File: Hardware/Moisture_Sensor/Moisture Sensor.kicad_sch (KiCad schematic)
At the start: 24 parts, among them J1 Conn_01x02_Pin, J2 Conn_01x02_Pin, J3 Conn_01x03_Pin, Q1 BSS123, Q2 BSS84, U1 ESP32-H2-SUPERMINI, U3 NE555D

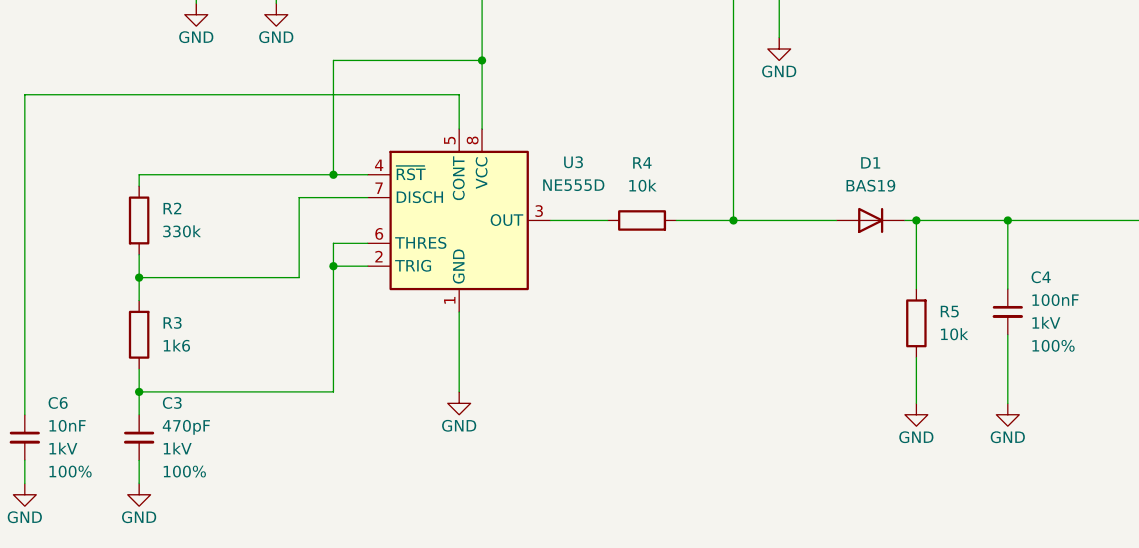
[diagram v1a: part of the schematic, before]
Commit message: R2 auf 330 geändert und R5 auf 1Meg
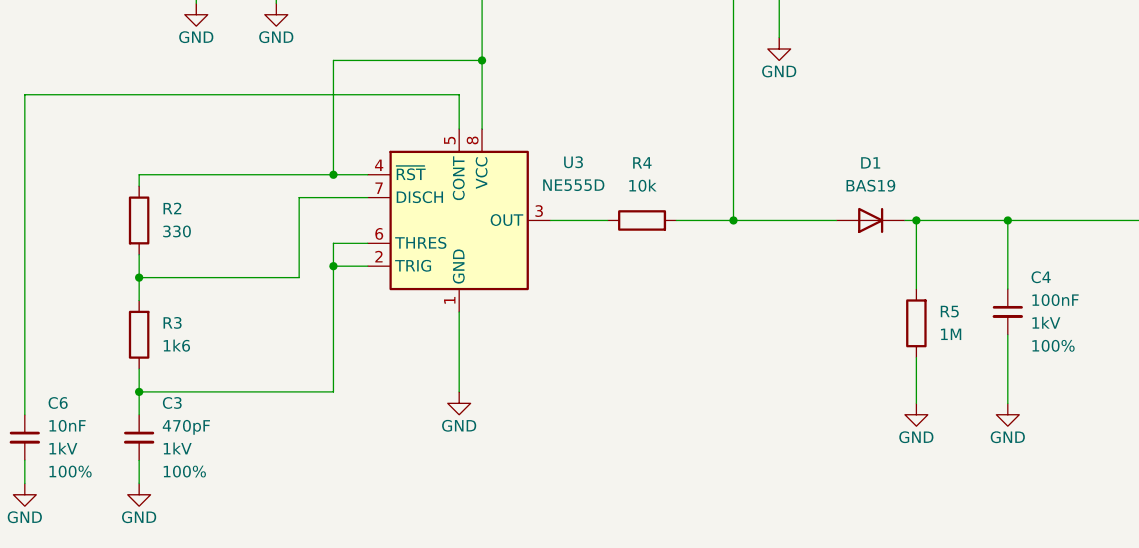
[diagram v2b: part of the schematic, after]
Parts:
- R2: value 330k -> 330
- R5: value 10k -> 1M
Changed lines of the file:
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@@
 			)
 		)
-		(property "Value" "330k"
+		(property "Value" "330"
 			(at 40.64 162.5599 0)
 			(effects
@@
 			)
 		)
-		(property "Value" "10k"
+		(property "Value" "1M"
 			(at 127 173.9899 0)
 			(effects

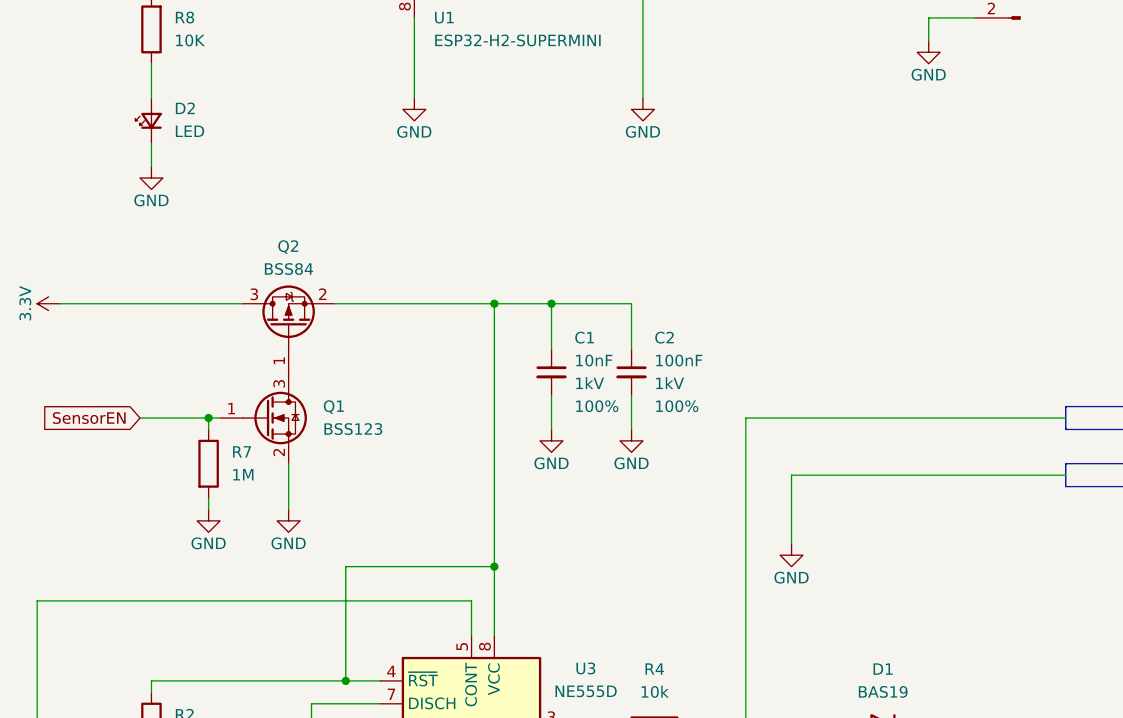
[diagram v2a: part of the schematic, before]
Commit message: Fehler im Schlatplan!!! R7, Q1 und Q2 nicht bestücken. Verbindung von Q1/pin1 zu Q2/Pin2 wie eingezeichnet herstellen und mit GPIO ein und ausschalten.
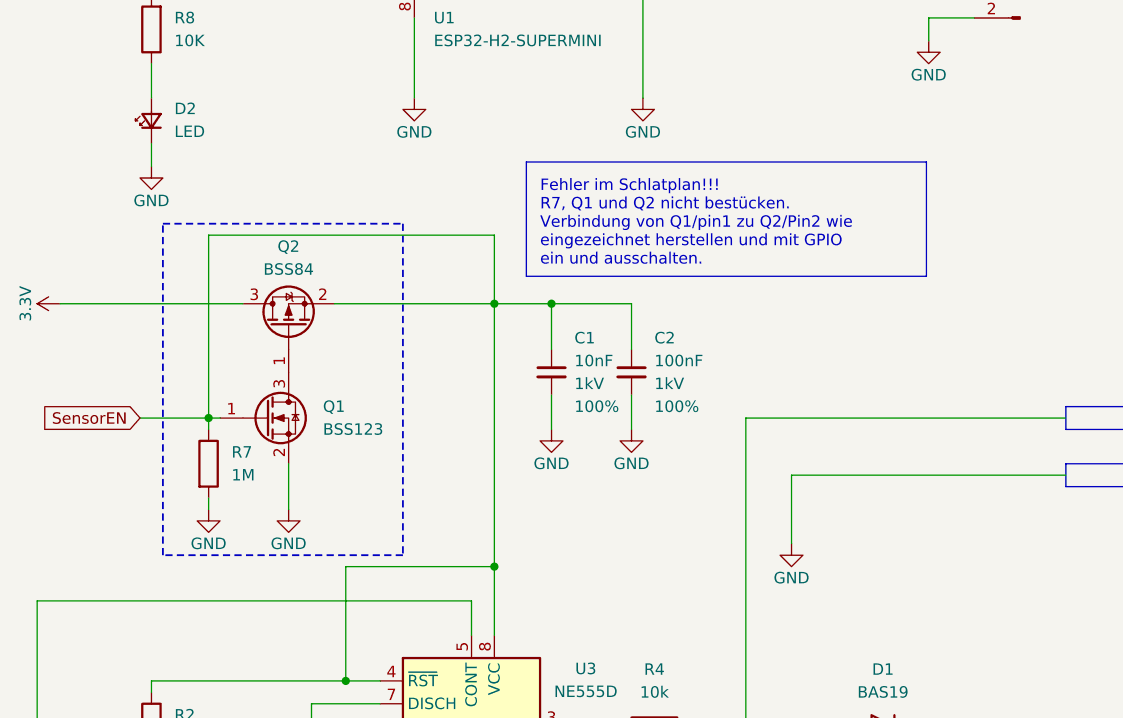
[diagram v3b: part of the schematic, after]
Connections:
- net SensorEN: now also C1.1, C2.1, Q2.2 (S), R2.1, U3.4 (~{RST}), U3.8 (VCC)
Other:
- note added: "Fehler im Schlatplan!!! R7, Q1 und Q2 nicht bestücken. Verbindung von Q1/pin1 zu Q2/Pin2 wie eingezeichnet herstellen und mit GPIO ein und ausschalten."
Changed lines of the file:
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@@
 	(paper "A4")
+	(rectangle
+		(start 39.37 105.41)
+		(end 66.04 142.24)
+		(stroke
+			(width 0.2)
+			(type dash)
+			(color 255 8 10 1)
+		)
+		(fill
+			(type none)
+		)
+	)
 	(rectangle
 		(start 139.7 132.08)
@@
 		)
 	)
+	(rectangle
+		(start 79.756 98.552)
+		(end 124.206 111.252)
+		(stroke
+			(width 0)
+			(type solid)
+		)
+		(fill
+			(type color)
+			(color 255 253 215 1)
+		)
+	)
+	(text "Fehler im Schlatplan!!!\nR7, Q1 und Q2 nicht bestücken.\nVerbindung von Q1/pin1 zu Q2/Pin2 wie\neingezeichnet herstellen und mit GPIO\nein und ausschalten."
+		(exclude_from_sim no)
+		(at 81.28 105.41 0)
+		(effects
+			(font
+				(size 1.27 1.27)
+				(color 255 12 12 1)
+			)
+			(justify left)
+		)
+	)
 	(junction
 		(at 38.1 180.34)
@@
 	(wire
 		(pts
+			(xy 76.2 106.68) (xy 76.2 114.3)
+		)
+		(stroke
+			(width 0.4)
+			(type dash)
+		)
+	)
+	(wire
+		(pts
 			(xy 111.76 57.15) (xy 125.73 57.15)
 		)
@@
 	(wire
 		(pts
+			(xy 44.45 127) (xy 44.45 106.68)
+		)
+		(stroke
+			(width 0.4)
+			(type dash)
+		)
+	)
+	(wire
+		(pts
 			(xy 67.31 91.44) (xy 67.31 82.55)
 		)
@@
 		)
 	)
+	(wire
+		(pts
+			(xy 44.45 106.68) (xy 76.2 106.68)
+		)
+		(stroke
+			(width 0.4)
+			(type dash)
+		)
+	)
